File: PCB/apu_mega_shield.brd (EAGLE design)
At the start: 105.4 x 54.4 mm, 39 parts, among them IC1 74AHC573, IC2 4050D, IC3 DS1307, IC4 LP298XS, Q1 32.768, U1 IS62C1024AL, X1 MICROSDMOLEX

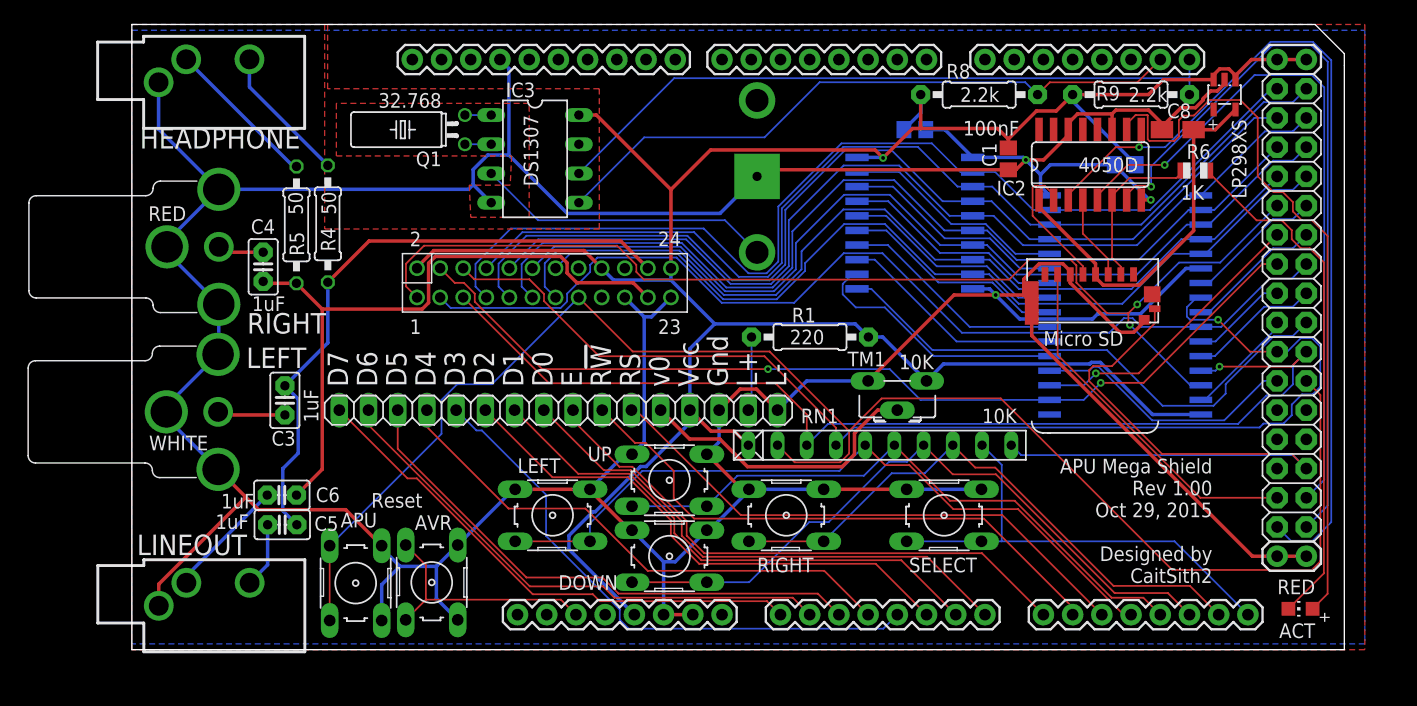
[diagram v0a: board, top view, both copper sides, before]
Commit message: All parts that are not buttons or connectors replaced with SMT equivalents. :)
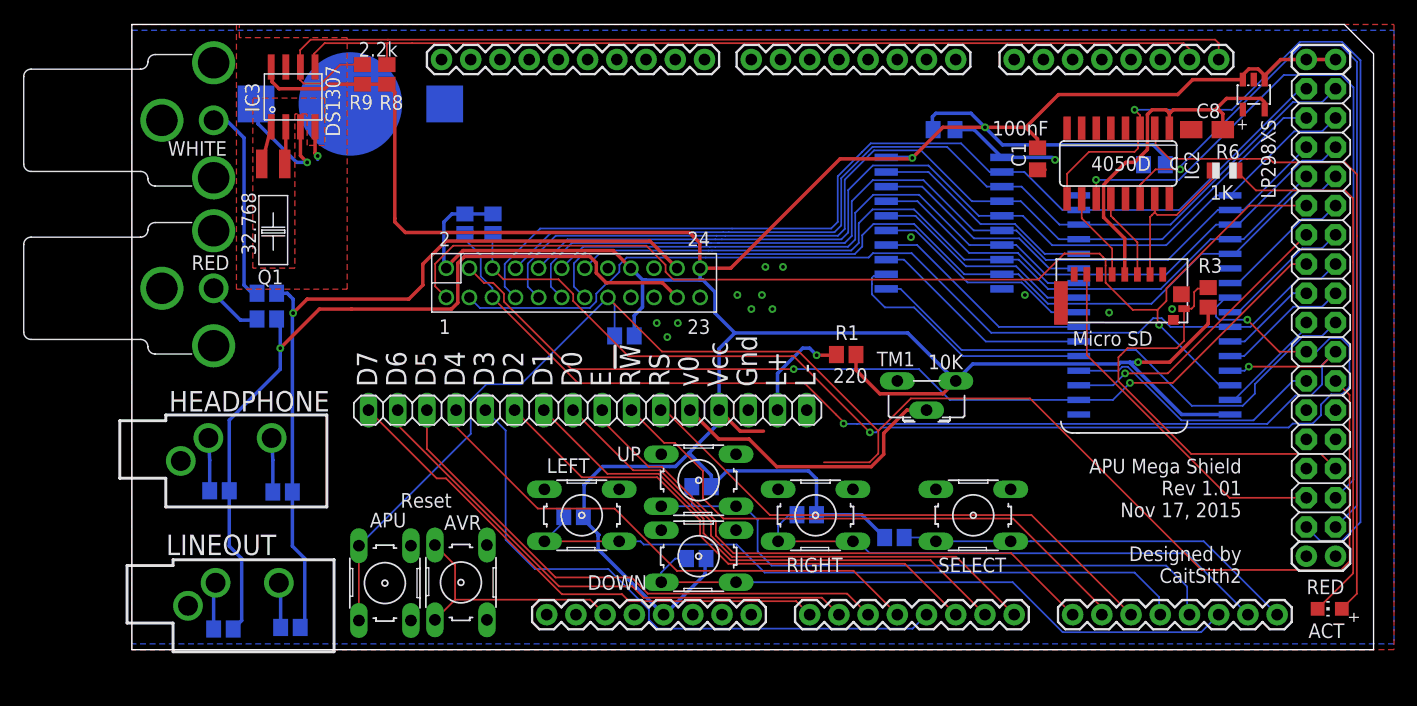
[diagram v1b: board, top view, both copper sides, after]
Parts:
- removed RN1: 10K, resistor-net:RN-10
- added R10, R11, R12, R13, R14, R15, R2, R3, R7: 10K, resistor:R0805
- BAT: device adafruit:CR1220-THM -> adafruit:CR1220-SMD
- C3, C4, C5, C6: device rcl-ez:C025-025X050 -> resistor:C0805
- IC3: device adafruit:DIL08 -> adafruit:SO-08
- Q1: device crystal:TC38H -> crystal:SMD
- R1, R8, R9: device adafruit:0207/10 -> resistor:R0805
- R4, R5: device rcl:0207/10 -> resistor:R0805
- moved R9 66.9 mm to (20.0, 50.0), turned to 90 degrees
- moved R8 51.5 mm to (22.2, 50.0), turned to 270 degrees
- moved BAT 35.9 mm to (19.0, 47.4), turned to 0 degrees
- moved U$2 33.0 mm to (8.96, 16.4)
- moved U$4 25.3 mm to (7.11, 46.0)
- moved R5 24.1 mm to (7.62, 13.8), flipped to the bottom, turned to 180 degrees
- moved R4 23.6 mm to (13.1, 13.7), flipped to the bottom, turned to 180 degrees
- moved IC3 21.7 mm to (14.0, 48.1), turned to 0 degrees
- moved Q1 17.5 mm to (12.3, 40.0)
- moved C6 12.7 mm to (7.96, 1.80), flipped to the bottom, turned to 0 degrees
- moved C3 9.44 mm to (11.7, 31.0), flipped to the bottom, turned to 0 degrees
- moved C5 8.96 mm to (13.8, 1.94), flipped to the bottom, turned to 0 degrees
- moved C4 4.55 mm to (11.7, 28.8), flipped to the bottom, turned to 0 degrees
- moved U$5 3.63 mm to (7.11, 31.4)
- moved R1 3.50 mm to (62.1, 25.7)
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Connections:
- removed net N$12: IC2.4, X1.3
- removed net N$39: BAT.+2, IC3.3
- removed net N$5: ACT.A, IC2.10
- removed net N$6: IC2.2, X1.5
- removed net N$7: IC2.6, R6.1, X1.2
- new net BUF_CLK: IC2.10, X1.5
- new net BUF_CS: IC2.15, R6.1, X1.2
- new net BUF_DI: IC2.12, X1.3
- new net BUF_LED: ACT.A, IC2.2
- new net N$15: BAT.+$1, BAT.+$2, IC3.3
- net !RD: now also R14.2; no longer RN1.4
- net !WR: now also R15.2; no longer RN1.3
- net CD: now also R3.2; no longer RN1.10
- net CS: now also IC2.14; no longer IC2.7
- net DI: now also IC2.11; no longer IC2.5
- net DOWN: now also R11.2; no longer RN1.7
- net GND: now also IC2.5, IC2.7; no longer IC2.11, IC2.14
- net LEFT: now also R13.2; no longer RN1.5
- net RIGHT: now also R10.2; no longer RN1.8
- net RST: now also R2.2; no longer RN1.2
- net SELECT: now also R7.2; no longer RN1.9
- net UP: now also R12.2; no longer RN1.6
- net VCC: now also R10.1, R11.1, R12.1, R13.1, R14.1, R15.1, R2.1, R3.1, R7.1; no longer RN1.1
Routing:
- net GND: track 427.1 -> 13.4 mm, vias 3 -> 15
- net VCC: track 214.6 -> 329.9 mm, vias 1 -> 3
- net N$5: track 64.1 -> 0.00 mm
- net BUF_LED: track 0.00 -> 58.4 mm
- net SCL: track 59.6 -> 90.6 mm
- net N$39: track 26.0 -> 0.00 mm
- net SDA: track 56.6 -> 80.7 mm
- net CD: track 58.1 -> 36.8 mm
- net ALEFT: track 54.5 -> 68.9 mm, vias 0 -> 1
- net N$7: track 14.3 -> 0.00 mm
- net ARIGHT: track 57.4 -> 71.4 mm, vias 0 -> 1
- net BUF_CS: track 0.00 -> 13.9 mm
- net N$6: track 12.1 -> 0.00 mm
- net N$2: track 5.92 -> 17.5 mm
- net N$15: track 0.00 -> 10.8 mm, vias 0 -> 1
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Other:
- board size 105.4 x 54.4 mm -> 108 x 54.4 mm
- board text added: "APU Mega Shield Rev 1.01 Nov 17, 2015 Designed by CaitSith2"
- board text removed: "APU Mega Shield Rev 1.00 Oct 29, 2015 Designed by CaitSith2"
- board text removed: "LEFT"
- board text removed: "RIGHT"

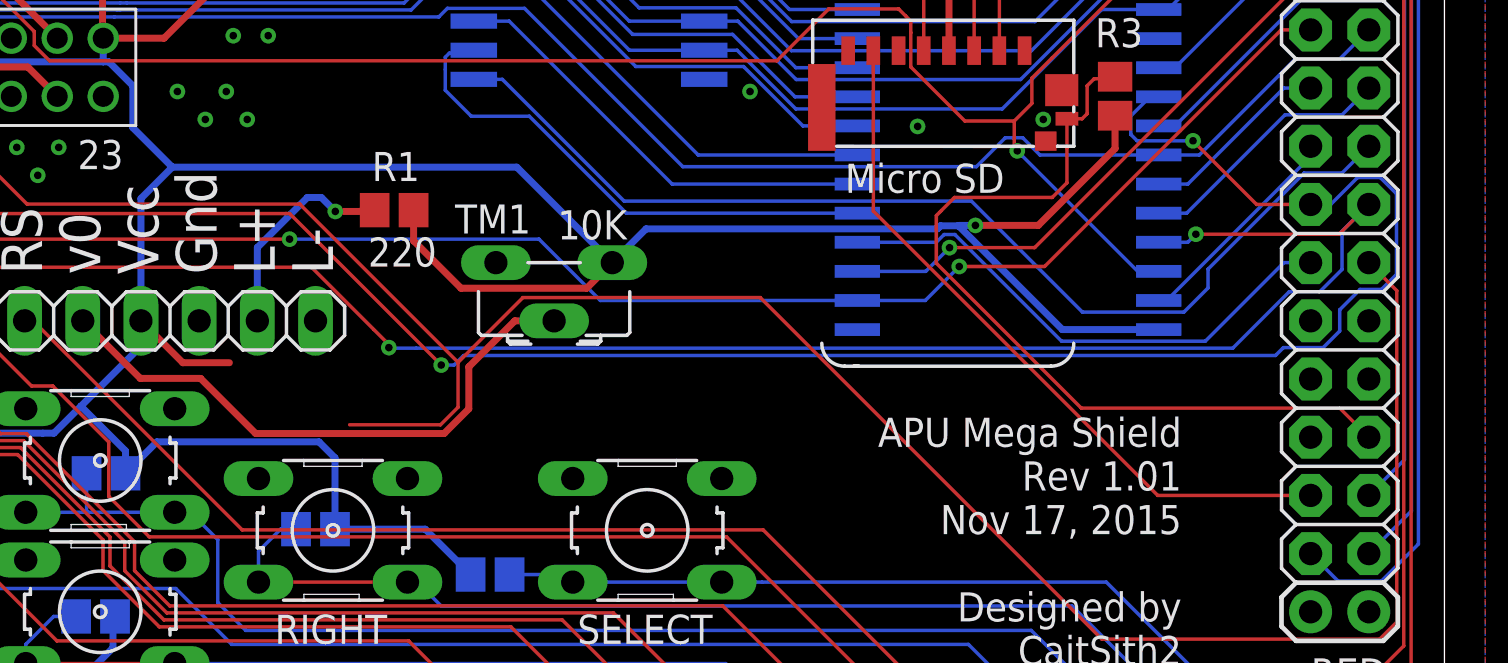
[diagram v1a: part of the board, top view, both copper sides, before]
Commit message: R1 removed from PCB. It was supposed to be the current limiting resistor for the LCD backlight, however, the LCD module in use already has a current limiting resistor mounted right on that module.
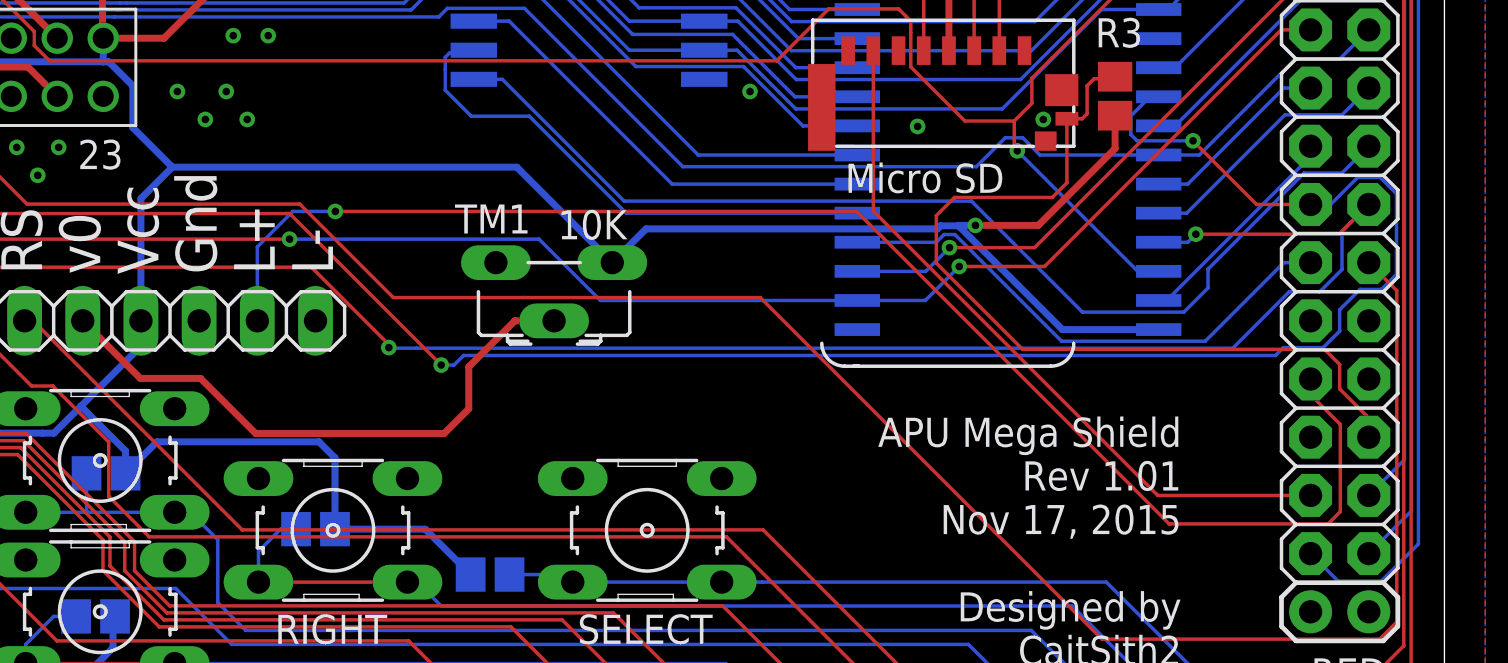
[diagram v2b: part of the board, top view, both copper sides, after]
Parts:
- removed R1: 220, resistor:R0805
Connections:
- net N$14: now also U$6.46; no longer R1.2
- net VCC: no longer R1.1
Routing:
- net N$14: track 9.50 -> 63.3 mm
- net VCC: track 329.9 -> 314.0 mm
- net RST: track 142.6 -> 133.2 mm
- net CD: track 36.8 -> 37.9 mm
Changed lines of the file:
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@@
 </element>
 <element name="X1" library="adafruit" package="MICROSD-1" value="MICROSDMOLEX" x="80.772" y="28.448"/>
-<element name="R1" library="resistor" package="R0805" value="220" x="62.105" y="25.6602" smashed="yes" rot="R180">
-<attribute name="NAME" x="63.2226" y="28.2002" size="1.27" layer="21" font="vector" ratio="16" rot="R180"/>
-<attribute name="VALUE" x="63.9592" y="24.4664" size="1.27" layer="21" font="vector" ratio="16" rot="R180"/>
-</element>
 <element name="R2" library="resistor" package="R0805" value="10K" x="42.8244" y="27.2796" smashed="yes" rot="MR0">
 <attribute name="NAME" x="43.8912" y="28.2956" size="1.27" layer="26" font="vector" ratio="16" rot="MR0"/>
@@
 <contactref element="APU" pad="3"/>
 <contactref element="APU" pad="4"/>
-<wire x1="64.8955" y1="19.0144" x2="57.9855" y2="25.9244" width="0.1524" layer="1"/>
 <wire x1="57.9855" y1="25.9244" x2="46.0821" y2="25.9244" width="0.1524" layer="1"/>
 <wire x1="46.0821" y1="25.9244" x2="41.3817" y2="30.6248" width="0.1524" layer="1"/>
@@
 <wire x1="29.464" y1="21.7216" x2="29.464" y2="18.7667" width="0.1524" layer="16"/>
 <wire x1="29.464" y1="18.7667" x2="19.7391" y2="9.0418" width="0.1524" layer="16"/>
-<wire x1="64.8955" y1="19.0144" x2="64.8955" y2="17.0556" width="0.1524" layer="1"/>
-<wire x1="64.8955" y1="17.0556" x2="64.1307" y2="16.2908" width="0.1524" layer="1"/>
-<wire x1="64.1307" y1="16.2908" x2="60.1632" y2="16.2908" width="0.1524" layer="1"/>
 <wire x1="104.648" y1="23.368" x2="105.8695" y2="22.1465" width="0.1524" layer="1"/>
 <wire x1="105.8695" y1="22.1465" x2="105.8695" y2="7.6776" width="0.1524" layer="1"/>
@@
 <wire x1="92.9953" y1="6.9358" x2="78.0867" y2="21.8444" width="0.1524" layer="1"/>
 <wire x1="78.0867" y1="21.8444" x2="67.7255" y2="21.8444" width="0.1524" layer="1"/>
-<wire x1="67.7255" y1="21.8444" x2="64.8955" y2="19.0144" width="0.1524" layer="1"/>
 <wire x1="19.7391" y1="9.0418" x2="19.7391" y2="2.5394" width="0.1524" layer="1"/>
 <contactref element="R2" pad="2"/>
 <wire x1="41.9744" y1="27.2796" x2="41.9744" y2="30.0321" width="0.1524" layer="16"/>
 <wire x1="41.9744" y1="30.0321" x2="41.3817" y2="30.6248" width="0.1524" layer="16"/>
+<wire x1="67.7255" y1="21.8444" x2="62.0655" y2="21.8444" width="0.1524" layer="1"/>
+<wire x1="62.0655" y1="21.8444" x2="57.9855" y2="25.9244" width="0.1524" layer="1"/>
 </signal>
 <signal name="A0">
@@
 <contactref element="IC4" pad="3"/>
 <contactref element="C1" pad="1"/>
-<contactref element="R1" pad="1"/>
 <wire x1="51.054" y1="20.828" x2="51.054" y2="19.7229" width="0.3048" layer="16"/>
 <wire x1="51.054" y1="19.7229" x2="48.43155" y2="17.10045" width="0.3048" layer="16"/>
@@
 <wire x1="44.6532" y1="32.1329" x2="44.4202" y2="32.1329" width="0.3048" layer="16"/>
 <wire x1="44.4202" y1="32.1329" x2="43.3883" y2="33.1648" width="0.3048" layer="16"/>
-<wire x1="51.054" y1="20.828" x2="52.8829" y2="18.9991" width="0.3048" layer="1"/>
-<wire x1="52.8829" y1="18.9991" x2="54.9149" y2="18.9991" width="0.3048" layer="1"/>
 <wire x1="65.5828" y1="42.799" x2="67.8032" y2="42.799" width="0.3048" layer="16"/>
 <wire x1="67.8032" y1="42.799" x2="67.8498" y2="42.7524" width="0.3048" layer="16"/>
@@
 <wire x1="77.8189" y1="45.3124" x2="77.7161" y2="45.4152" width="0.3048" layer="1"/>
 <wire x1="77.7161" y1="45.4152" x2="74.168" y2="45.4152" width="0.3048" layer="1"/>
-<wire x1="62.955" y1="25.6602" x2="62.955" y2="24.3194" width="0.3048" layer="1"/>
-<wire x1="62.955" y1="24.3194" x2="65.024" y2="22.2504" width="0.3048" layer="1"/>
-<wire x1="65.024" y1="22.2504" x2="70.5104" y2="22.2504" width="0.3048" layer="1"/>
-<wire x1="70.5104" y1="22.2504" x2="71.628" y2="23.368" width="0.3048" layer="1"/>
 <wire x1="52.4228" y1="27.5364" x2="67.4596" y2="27.5364" width="0.3048" layer="16"/>
 <wire x1="67.4596" y1="27.5364" x2="71.628" y2="23.368" width="0.3048" layer="16"/>
@@
 <wire x1="91.472" y1="29.648" x2="91.472" y2="28.3742" width="0.1524" layer="1"/>
 <wire x1="85.7715" y1="24.3125" x2="85.7715" y2="23.3471" width="0.1524" layer="1"/>
-<wire x1="85.7715" y1="23.3471" x2="92.1006" y2="17.018" width="0.1524" layer="1"/>
-<wire x1="92.1006" y1="17.018" x2="103.378" y2="17.018" width="0.1524" layer="1"/>
-<wire x1="103.378" y1="17.018" x2="104.648" y2="15.748" width="0.1524" layer="1"/>
+<wire x1="85.7715" y1="23.3471" x2="89.4589" y2="19.6597" width="0.1524" layer="1"/>
 <contactref element="R3" pad="2"/>
 <wire x1="91.472" y1="29.648" x2="92.132" y2="29.648" width="0.1524" layer="1"/>
@@
 <wire x1="85.9536" y1="25.6032" x2="85.7715" y2="25.4211" width="0.1524" layer="1"/>
 <wire x1="85.7715" y1="25.4211" x2="85.7715" y2="24.3125" width="0.1524" layer="1"/>
+<wire x1="103.378" y1="18.923" x2="102.7176" y2="19.5834" width="0.1524" layer="1"/>
+<wire x1="102.7176" y1="19.5834" x2="89.5352" y2="19.5834" width="0.1524" layer="1"/>
+<wire x1="89.5352" y1="19.5834" x2="89.4589" y2="19.6597" width="0.1524" layer="1"/>
+<wire x1="103.378" y1="18.923" x2="103.378" y2="17.8562" width="0.1524" layer="1"/>
+<wire x1="103.378" y1="17.8562" x2="104.5464" y2="16.6878" width="0.1524" layer="1"/>
+<wire x1="104.5464" y1="16.6878" x2="104.5464" y2="15.8496" width="0.1524" layer="1"/>
+<wire x1="104.5464" y1="15.8496" x2="104.648" y2="15.748" width="0.1524" layer="1"/>
 </signal>
 <signal name="DO">
@@
 <signal name="N$14">
 <contactref element="JP1" pad="15"/>
-<contactref element="R1" pad="2"/>
-<wire x1="56.134" y1="20.828" x2="56.134" y2="24.0284" width="0.3048" layer="16"/>
-<wire x1="56.134" y1="24.0284" x2="58.3184" y2="26.2128" width="0.3048" layer="16"/>
-<wire x1="58.3184" y1="26.2128" x2="58.928" y2="26.2128" width="0.3048" layer="16"/>
-<wire x1="58.928" y1="26.2128" x2="59.5376" y2="25.6032" width="0.3048" layer="16"/>
 <via x="59.5376" y="25.6032" extent="1-16" drill="0.3302"/>
-<wire x1="59.5376" y1="25.6032" x2="61.198" y2="25.6032" width="0.3048" layer="1"/>
-<wire x1="61.198" y1="25.6032" x2="61.255" y2="25.6602" width="0.3048" layer="1"/>
+<contactref element="U$6" pad="46"/>
+<wire x1="102.108" y1="18.288" x2="102.108" y2="17.6022" width="0.1524" layer="1"/>
+<wire x1="102.108" y1="17.6022" x2="103.4034" y2="16.3068" width="0.1524" layer="1"/>
+<wire x1="103.4034" y1="16.3068" x2="103.4034" y2="12.4968" width="0.1524" layer="1"/>
+<wire x1="103.4034" y1="12.4968" x2="102.87" y2="11.9634" width="0.1524" layer="1"/>
+<wire x1="102.87" y1="11.9634" x2="95.9358" y2="11.9634" width="0.1524" layer="1"/>
+<wire x1="95.9358" y1="11.9634" x2="82.296" y2="25.6032" width="0.1524" layer="1"/>
+<wire x1="56.134" y1="20.828" x2="56.134" y2="24.0538" width="0.1524" layer="16"/>
+<wire x1="56.134" y1="24.0538" x2="57.6834" y2="25.6032" width="0.1524" layer="16"/>
+<wire x1="57.6834" y1="25.6032" x2="59.5376" y2="25.6032" width="0.1524" layer="16"/>
+<wire x1="82.296" y1="25.6032" x2="59.5376" y2="25.6032" width="0.1524" layer="1"/>
 </signal>
 <signal name="N$15">
